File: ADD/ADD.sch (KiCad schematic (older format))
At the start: 15 parts, among them J1 Conn_01x08_Male, J2 Conn_01x08_Male, J3 Conn_01x08_Male, J4 Conn_01x05_Male, J5 Conn_01x01_Male, J6 Conn_01x01_Male, U1 74LS283, U2 74LS283, U3 74LS573, U4 74AHC1G08

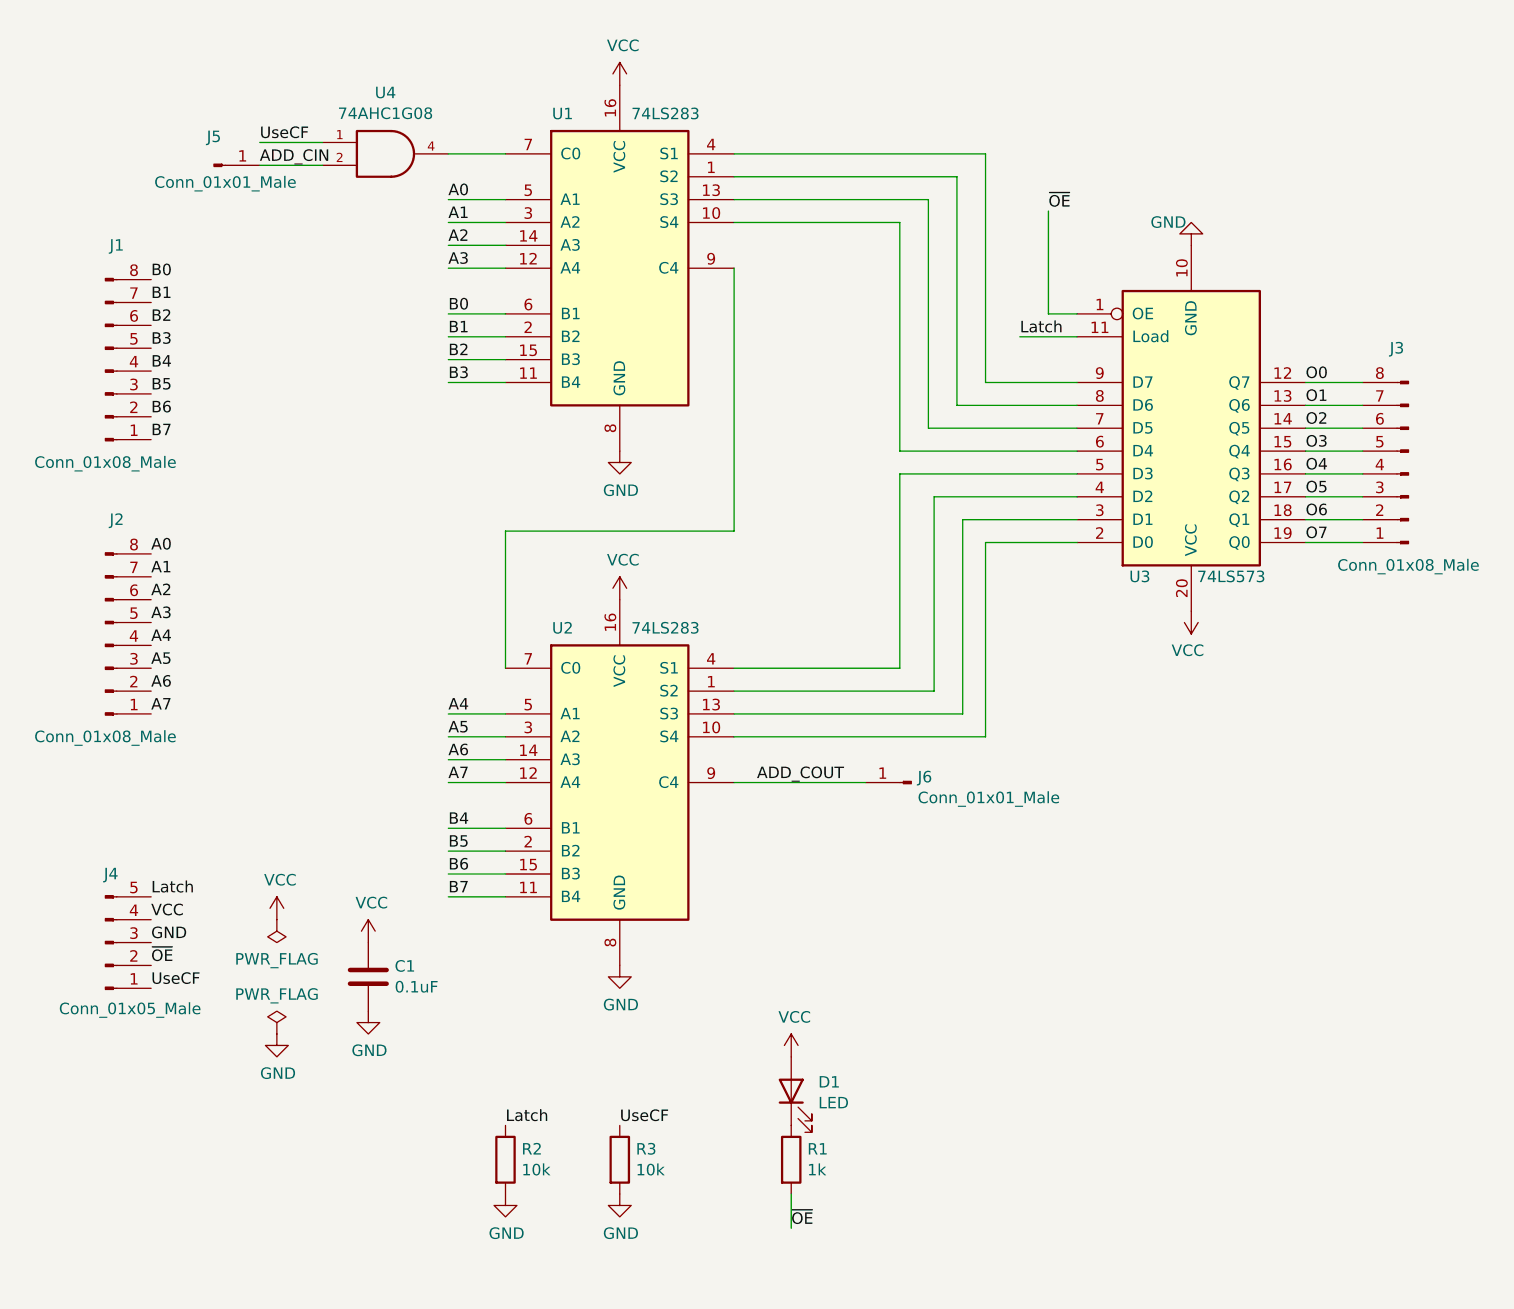
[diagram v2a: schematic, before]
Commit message: Add NAND to ADD cmd
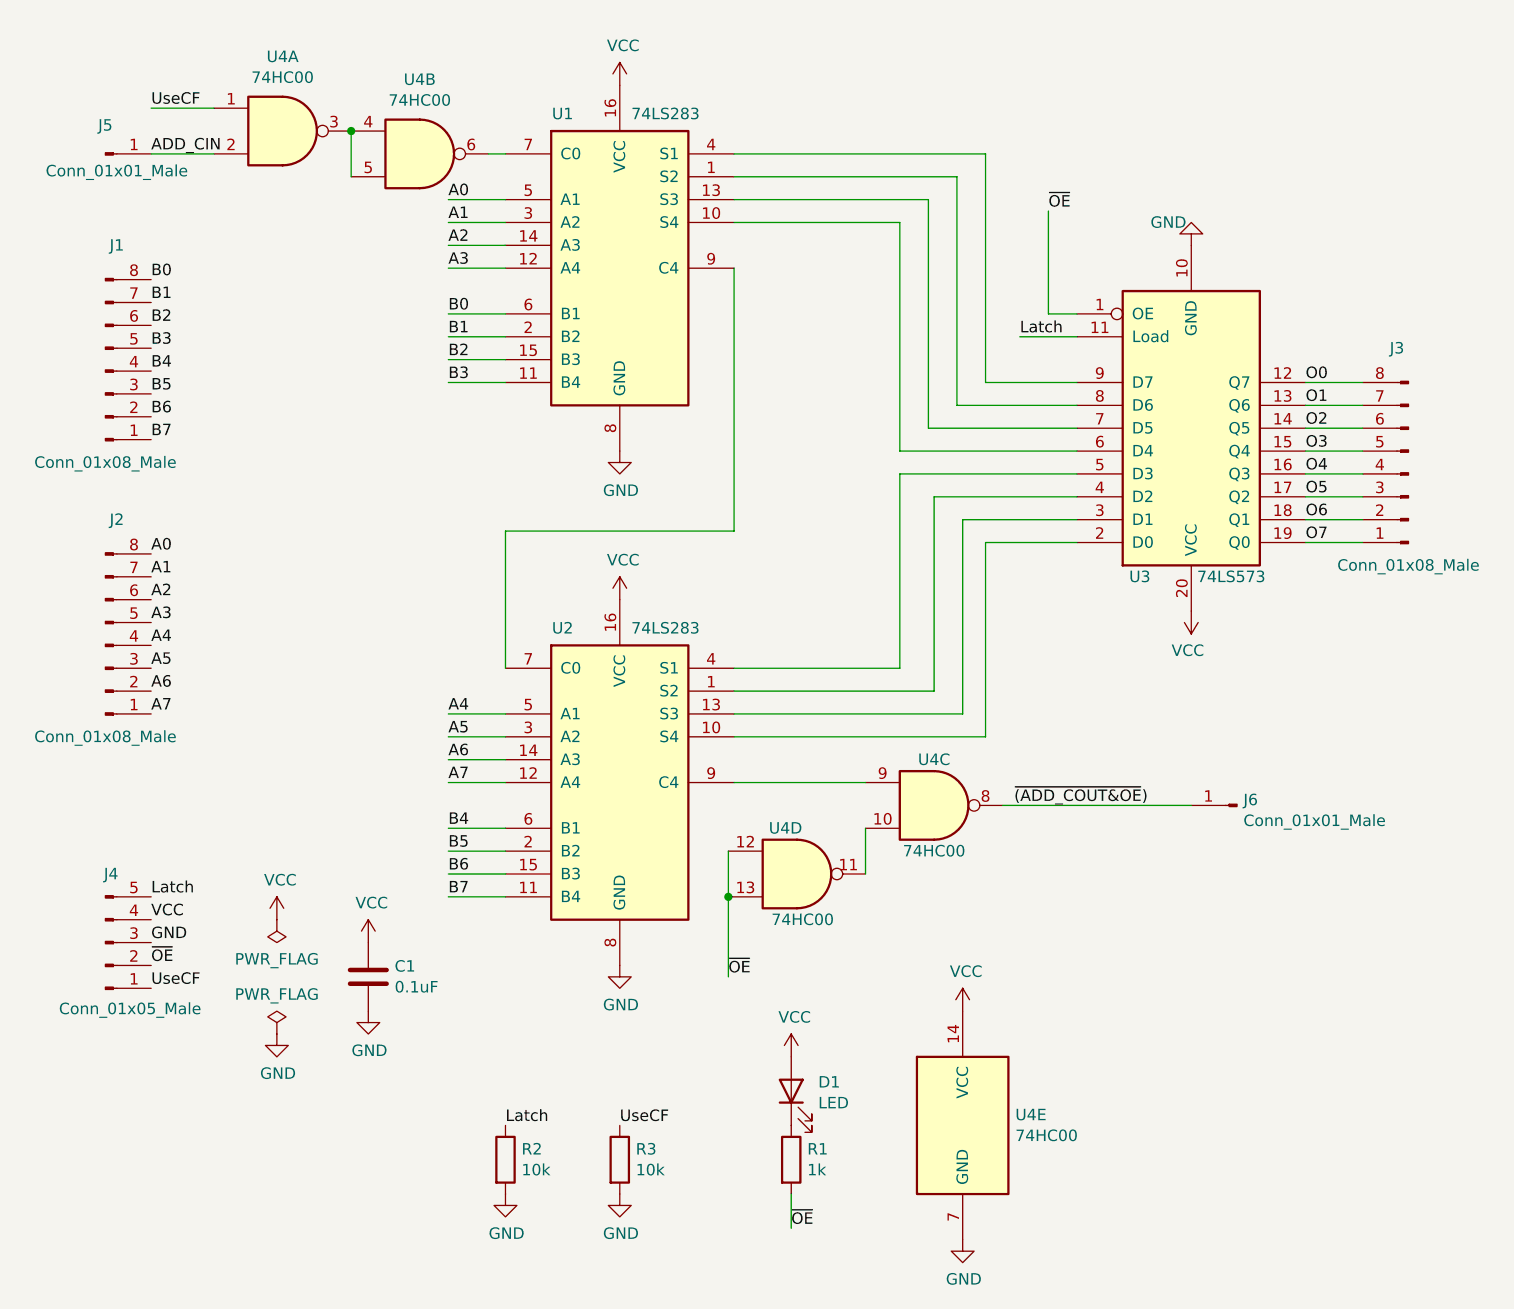
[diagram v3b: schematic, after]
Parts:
- removed U4: 74AHC1G08, CommonLibrary:tssop5, symbol 74xGxx:74AHC1G08
- added U4: 74HC00, Package_DIP:DIP-14_W7.62mm, symbol 74xx:74HC00
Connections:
- net ADD_CIN: now also U4.2
- net GND: now also U4.7 (GND)
- net UseCF: now also U4.1
- net VCC: now also U4.14 (VCC)
- net ~OE: now also U4.12, U4.13
- net at U1.7 (C0): now also U4.6
- net ADD_COUT: no longer names the net of U2.9 (C4)
- net ADD_COUT: now also U4.9; no longer J6.1 (Pin_1)
- new net: U4.3, U4.4, U4.5
- new net: U4.10, U4.11
- new net ~(ADD_COUT&OE): J6.1 (Pin_1), U4.8
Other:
- moved on the sheet: J5, J6
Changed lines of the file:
@@
 L Connector:Conn_01x01_Male J5
 U 1 1 62B23640
-P 1475 1800
-F 0 "J5" H 1475 1925 50  0000 C CNN
-F 1 "Conn_01x01_Male" H 1525 1725 50  0000 C CNN
-F 2 "Connector_PinHeader_2.54mm:PinHeader_1x01_P2.54mm_Vertical" H 1475 1800 50  0001 C CNN
-F 3 "~" H 1475 1800 50  0001 C CNN
-	1    1475 1800
+P 1000 1750
+F 0 "J5" H 1000 1875 50  0000 C CNN
+F 1 "Conn_01x01_Male" H 1050 1675 50  0000 C CNN
+F 2 "Connector_PinHeader_2.54mm:PinHeader_1x01_P2.54mm_Vertical" H 1000 1750 50  0001 C CNN
+F 3 "~" H 1000 1750 50  0001 C CNN
+	1    1000 1750
 	1    0    0    -1
 $EndComp
@@
 L Connector:Conn_01x01_Male J6
 U 1 1 62B24097
-P 4525 4500
-F 0 "J6" H 4497 4524 50  0000 R CNN
-F 1 "Conn_01x01_Male" H 4497 4433 50  0000 R CNN
-F 2 "Connector_PinHeader_2.54mm:PinHeader_1x01_P2.54mm_Vertical" H 4525 4500 50  0001 C CNN
-F 3 "~" H 4525 4500 50  0001 C CNN
-	1    4525 4500
+P 5950 4600
+F 0 "J6" H 5922 4624 50  0000 R CNN
+F 1 "Conn_01x01_Male" H 5922 4533 50  0000 R CNN
+F 2 "Connector_PinHeader_2.54mm:PinHeader_1x01_P2.54mm_Vertical" H 5950 4600 50  0001 C CNN
+F 3 "~" H 5950 4600 50  0001 C CNN
+	1    5950 4600
 	-1   0    0    -1
 $EndComp
 Wire Wire Line
 	3750 4500 4325 4500
-Text Label 3850 4500 0    50   ~ 0
-ADD_COUT
+Text Label 4975 4600 0    50   ~ 0
+~(ADD_COUT&OE)
 Text Label 5125 2000 0    50   ~ 0
 ~OE
@@
 	-1   0    0    1
 $EndComp
-$Comp
-L 74xGxx:74AHC1G08 U4
-U 1 1 62B312EB
-P 2250 1750
-F 0 "U4" H 2225 2017 50  0000 C CNN
-F 1 "74AHC1G08" H 2225 1926 50  0000 C CNN
-F 2 "CommonLibrary:tssop5" H 2250 1750 50  0001 C CNN
-F 3 "http://www.ti.com/lit/sg/scyt129e/scyt129e.pdf" H 2250 1750 50  0001 C CNN
-	1    2250 1750
-	1    0    0    -1
-$EndComp
-Text Label 1675 1700 0    50   ~ 0
+Text Label 1200 1550 0    50   ~ 0
 UseCF
-Text Label 1675 1800 0    50   ~ 0
+Text Label 1200 1750 0    50   ~ 0
 ADD_CIN
 Wire Wire Line
-	1675 1700 1950 1700
-Wire Wire Line
-	1675 1800 1950 1800
+	1200 1550 1475 1550
+Wire Wire Line
+	1200 1750 1475 1750
 $Comp
 L power:VCC #PWR0103
@@
 	-1   0    0    1
 $EndComp
-Wire Wire Line
-	2500 1750 2750 1750
 $Comp
 L Device:C C1
@@
 Text Label 3250 6000 0    50   ~ 0
 UseCF
+$Comp
+L 74xx:74HC00 U4
+U 1 1 6381ABFB
+P 1775 1650
+F 0 "U4" H 1775 1975 50  0000 C CNN
+F 1 "74HC00" H 1775 1884 50  0000 C CNN
+F 2 "Package_DIP:DIP-14_W7.62mm" H 1775 1650 50  0001 C CNN
+F 3 "http://www.ti.com/lit/gpn/sn74hc00" H 1775 1650 50  0001 C CNN
+	1    1775 1650
+	1    0    0    -1
+$EndComp
+$Comp
+L 74xx:74HC00 U4
+U 2 1 6381C2B0
+P 2375 1750
+F 0 "U4" H 2375 2075 50  0000 C CNN
+F 1 "74HC00" H 2375 1984 50  0000 C CNN
+F 2 "Package_DIP:DIP-14_W7.62mm" H 2375 1750 50  0001 C CNN
+F 3 "http://www.ti.com/lit/gpn/sn74hc00" H 2375 1750 50  0001 C CNN
+	2    2375 1750
+	1    0    0    -1
+$EndComp
+$Comp
+L 74xx:74HC00 U4
+U 3 1 6381E198
+P 4625 4600
+F 0 "U4" H 4625 4800 50  0000 C CNN
+F 1 "74HC00" H 4625 4400 50  0000 C CNN
+F 2 "Package_DIP:DIP-14_W7.62mm" H 4625 4600 50  0001 C CNN
+F 3 "http://www.ti.com/lit/gpn/sn74hc00" H 4625 4600 50  0001 C CNN
+	3    4625 4600
+	1    0    0    -1
+$EndComp
+$Comp
+L 74xx:74HC00 U4
+U 4 1 6381F952
+P 4025 4900
+F 0 "U4" H 3975 5100 50  0000 C CNN
+F 1 "74HC00" H 4050 4700 50  0000 C CNN
+F 2 "Package_DIP:DIP-14_W7.62mm" H 4025 4900 50  0001 C CNN
+F 3 "http://www.ti.com/lit/gpn/sn74hc00" H 4025 4900 50  0001 C CNN
+	4    4025 4900
+	1    0    0    -1
+$EndComp
+$Comp
+L 74xx:74HC00 U4
+U 5 1 63820A9A
+P 4750 6000
+F 0 "U4" H 4980 6046 50  0000 L CNN
+F 1 "74HC00" H 4980 5955 50  0000 L CNN
+F 2 "Package_DIP:DIP-14_W7.62mm" H 4750 6000 50  0001 C CNN
+F 3 "http://www.ti.com/lit/gpn/sn74hc00" H 4750 6000 50  0001 C CNN
+	5    4750 6000
+	1    0    0    -1
+$EndComp
+Wire Wire Line
+	2675 1750 2750 1750
+Wire Wire Line
+	2075 1850 2075 1650
+Connection ~ 2075 1650
+Wire Wire Line
+	4325 4700 4325 4900
+Wire Wire Line
+	3725 4800 3725 5000
+Wire Wire Line
+	3725 5000 3725 5350
+Connection ~ 3725 5000
+Text Label 3725 5350 0    50   ~ 0
+~OE
+$Comp
+L power:VCC #PWR0109
+U 1 1 638433A8
+P 4750 5500
+F 0 "#PWR0109" H 4750 5350 50  0001 C CNN
+F 1 "VCC" H 4765 5673 50  0000 C CNN
+F 2 "" H 4750 5500 50  0001 C CNN
+F 3 "" H 4750 5500 50  0001 C CNN
+	1    4750 5500
+	1    0    0    -1
+$EndComp
+$Comp
+L power:GND #PWR0110
+U 1 1 63843816
+P 4750 6500
+F 0 "#PWR0110" H 4750 6250 50  0001 C CNN
+F 1 "GND" H 4755 6327 50  0000 C CNN
+F 2 "" H 4750 6500 50  0001 C CNN
+F 3 "" H 4750 6500 50  0001 C CNN
+	1    4750 6500
+	1    0    0    -1
+$EndComp
+Wire Wire Line
+	4925 4600 5750 4600
 $EndSCHEMATC

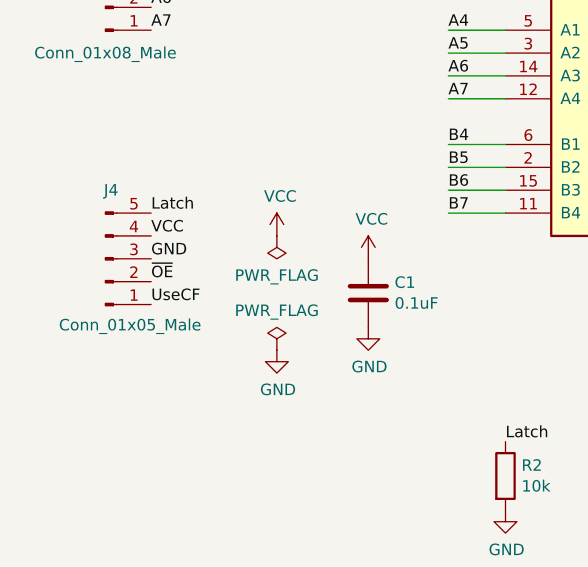
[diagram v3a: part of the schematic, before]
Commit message: Swap UseCF & OE
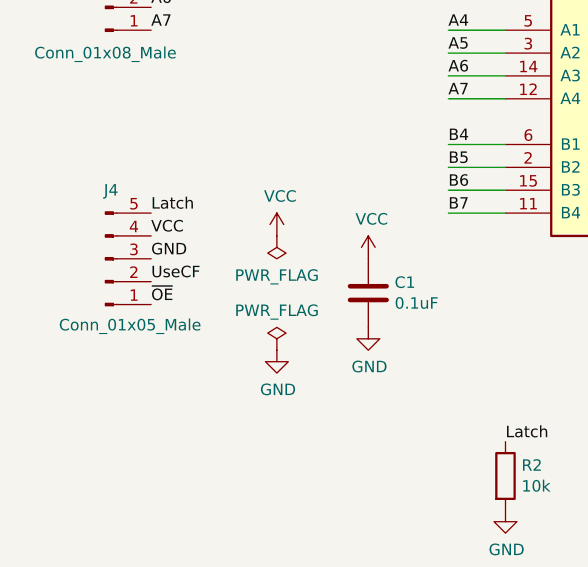
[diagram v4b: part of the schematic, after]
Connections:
- net UseCF: now also J4.2 (Pin_2); no longer J4.1 (Pin_1)
- net ~OE: now also J4.1 (Pin_1); no longer J4.2 (Pin_2)
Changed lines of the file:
@@
 	1    0    0    1
 $EndComp
+Text Label 1200 5300 0    50   ~ 0
+UseCF
 Text Label 1200 5400 0    50   ~ 0
-UseCF
-Text Label 1200 5300 0    50   ~ 0
 ~OE
 $Comp

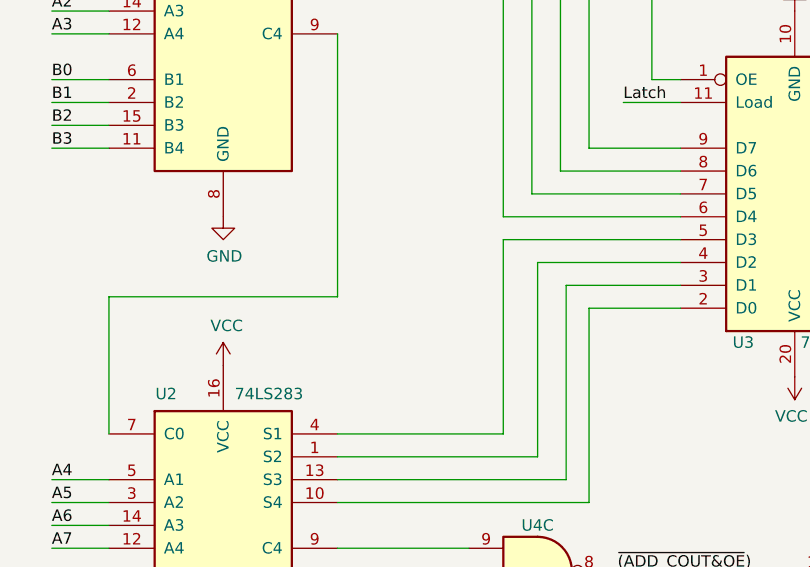
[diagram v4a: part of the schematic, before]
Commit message: Add auxiliary CF
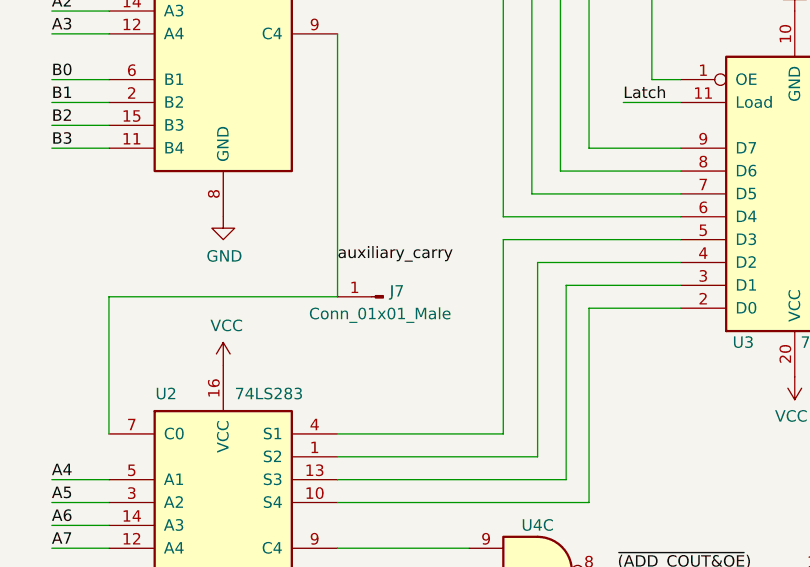
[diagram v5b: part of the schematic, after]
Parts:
- added J7: Conn_01x01_Male, Connector_PinHeader_2.54mm:PinHeader_1x01_P2.54mm_Vertical, symbol Connector:Conn_01x01_Male
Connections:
- net auxiliary_carry: now reaches U1.9 (C4), U2.7 (C0)
- net auxiliary_carry: now also J7.1 (Pin_1)
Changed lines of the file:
@@
 Wire Wire Line
 	4925 4600 5750 4600
+$Comp
+L Connector:Conn_01x01_Male J7
+U 1 1 64A73E8E
+P 3950 3400
+F 0 "J7" H 3922 3424 50  0000 R CNN
+F 1 "Conn_01x01_Male" H 4275 3325 50  0000 R CNN
+F 2 "Connector_PinHeader_2.54mm:PinHeader_1x01_P2.54mm_Vertical" H 3950 3400 50  0001 C CNN
+F 3 "~" H 3950 3400 50  0001 C CNN
+	1    3950 3400
+	-1   0    0    -1
+$EndComp
+Text Label 3750 3250 0    50   ~ 0
+auxiliary_carry
 $EndSCHEMATC
